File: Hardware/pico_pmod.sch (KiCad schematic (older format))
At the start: 6 parts, among them J1 Conn_02x15_Odd_Even, U1 Pico

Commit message: add power pin headers and initial layout work
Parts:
- J? (x3): footprint (none) -> Connector_PinHeader_2.54mm:PinHeader_1x02_P2.54mm_Vertical
- J?: value Conn_01x02 -> Conn_01x03; footprint (none) -> Connector_PinHeader_2.54mm:PinHeader_1x03_P2.54mm_Vertical; symbol Connector_Generic:Conn_01x02 -> Connector_Generic:Conn_01x03
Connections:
- net +3V3: now also J?.1 (Pin_1), J?.3 (Pin_3)
- net +5V: now also J?.1 (Pin_1), J?.1 (Pin_1)
- net GND: now also J?.1 (Pin_1)
- net Pic_VSYS renamed Pico_VSYS
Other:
- note added: "3V3_en connects to the SMPS enable pin\nto de-power the pico pull to ground\n(Pi Pico Datasheet, Page 8)"
- note added: "Direct input from the \nMicro USB connector approx 5v"
- note added: "Main System input voltage, \ncan be in the range of 1.8V to 5.5V"
- note added: "The main 3v3 supply from the pico, \nupto 300mA max draw"
- moved on the sheet: J?
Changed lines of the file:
@@
 Text GLabel 6650 4400 2    50   Input ~ 0
 Pico_3V3
-Text GLabel 8150 4400 2    50   Input ~ 0
+Text GLabel 9100 4500 2    50   Input ~ 0
 Pico_3v3_EN
 $Comp
 L Connector_Generic:Conn_01x02 J?
 U 1 1 607A9E26
-P 7950 4200
-F 0 "J?" V 7950 4400 50  0000 R CNN
-F 1 "Conn_01x02" V 7950 3950 50  0000 R CNN
-F 2 "" H 7950 4200 50  0001 C CNN
-F 3 "~" H 7950 4200 50  0001 C CNN
-	1    7950 4200
+P 8900 4300
+F 0 "J?" V 8900 4500 50  0000 R CNN
+F 1 "Conn_01x02" V 8900 4050 50  0000 R CNN
+F 2 "Connector_PinHeader_2.54mm:PinHeader_1x02_P2.54mm_Vertical" H 8900 4300 50  0001 C CNN
+F 3 "~" H 8900 4300 50  0001 C CNN
+	1    8900 4300
 	0    -1   -1   0
 $EndComp
@@
 F 0 "J?" V 6400 4400 50  0000 R CNN
 F 1 "Conn_01x02" V 6400 3950 50  0000 R CNN
-F 2 "" H 6400 4200 50  0001 C CNN
+F 2 "Connector_PinHeader_2.54mm:PinHeader_1x02_P2.54mm_Vertical" H 6400 4200 50  0001 C CNN
 F 3 "~" H 6400 4200 50  0001 C CNN
 	1    6400 4200
@@
 Pico_VBUS
 Text GLabel 4650 1800 2    50   Input ~ 0
-Pic_VSYS
+Pico_VSYS
 Wire Wire Line
 	4400 1700 4650 1700
@@
 	6500 4400 6650 4400
 Wire Wire Line
-	8050 4400 8150 4400
-Text GLabel 8200 5100 2    50   Input ~ 0
+	9000 4500 9100 4500
+Text GLabel 6600 5900 2    50   Input ~ 0
 Pico_VBUS
-Text GLabel 6650 5150 2    50   Input ~ 0
-Pic_VSYS
-$Comp
-L Connector_Generic:Conn_01x02 J?
+Text GLabel 9050 5750 3    50   Input ~ 0
+Pico_VSYS
+$Comp
+L Connector_Generic:Conn_01x03 J?
 U 1 1 607BB4AD
-P 6400 4950
-F 0 "J?" V 6400 5150 50  0000 R CNN
-F 1 "Conn_01x02" V 6400 4700 50  0000 R CNN
-F 2 "" H 6400 4950 50  0001 C CNN
-F 3 "~" H 6400 4950 50  0001 C CNN
-	1    6400 4950
+P 9050 5550
+F 0 "J?" V 9050 5750 50  0000 R CNN
+F 1 "Conn_01x03" V 9050 5300 50  0000 R CNN
+F 2 "Connector_PinHeader_2.54mm:PinHeader_1x03_P2.54mm_Vertical" H 9050 5550 50  0001 C CNN
+F 3 "~" H 9050 5550 50  0001 C CNN
+	1    9050 5550
 	0    -1   -1   0
 $EndComp
@@
 L Connector_Generic:Conn_01x02 J?
 U 1 1 607BCE20
-P 7950 4900
-F 0 "J?" V 7950 5100 50  0000 R CNN
-F 1 "Conn_01x02" V 7950 4650 50  0000 R CNN
-F 2 "" H 7950 4900 50  0001 C CNN
-F 3 "~" H 7950 4900 50  0001 C CNN
-	1    7950 4900
-	0    -1   -1   0
-$EndComp
-Wire Wire Line
-	6650 5150 6500 5150
-Wire Wire Line
-	8200 5100 8050 5100
+P 6350 5700
+F 0 "J?" V 6350 5900 50  0000 R CNN
+F 1 "Conn_01x02" V 6350 5450 50  0000 R CNN
+F 2 "Connector_PinHeader_2.54mm:PinHeader_1x02_P2.54mm_Vertical" H 6350 5700 50  0001 C CNN
+F 3 "~" H 6350 5700 50  0001 C CNN
+	1    6350 5700
+	0    -1   -1   0
+$EndComp
+Wire Wire Line
+	6600 5900 6450 5900
 Text GLabel 6800 3250 0    50   Input ~ 0
 GPIO_14
@@
 Wire Wire Line
 	7100 2150 6800 2150
+$Comp
+L power:+5V #PWR?
+U 1 1 60789CE8
+P 8700 5750
+F 0 "#PWR?" H 8700 5600 50  0001 C CNN
+F 1 "+5V" V 8715 5878 50  0000 L CNN
+F 2 "" H 8700 5750 50  0001 C CNN
+F 3 "" H 8700 5750 50  0001 C CNN
+	1    8700 5750
+	0    -1   -1   0
+$EndComp
+Text Notes 5800 6150 0    50   ~ 0
+Direct input from the \nMicro USB connector approx 5v
+Text Notes 8650 6400 0    50   ~ 0
+Main System input voltage, \ncan be in the range of 1.8V to 5.5V
+Text Notes 8600 4850 0    50   ~ 0
+3V3_en connects to the SMPS enable pin\nto de-power the pico pull to ground\n(Pi Pico Datasheet, Page 8)
+Text Notes 5900 4750 0    50   ~ 0
+The main 3v3 supply from the pico, \nupto 300mA max draw
+$Comp
+L power:+3.3V #PWR?
+U 1 1 607A1448
+P 9350 5750
+F 0 "#PWR?" H 9350 5600 50  0001 C CNN
+F 1 "+3.3V" V 9365 5878 50  0000 L CNN
+F 2 "" H 9350 5750 50  0001 C CNN
+F 3 "" H 9350 5750 50  0001 C CNN
+	1    9350 5750
+	0    1    1    0
+$EndComp
+Wire Wire Line
+	9150 5750 9350 5750
+Wire Wire Line
+	8950 5750 8700 5750
+$Comp
+L power:+5V #PWR?
+U 1 1 607A75D5
+P 6200 5900
+F 0 "#PWR?" H 6200 5750 50  0001 C CNN
+F 1 "+5V" V 6215 6028 50  0000 L CNN
+F 2 "" H 6200 5900 50  0001 C CNN
+F 3 "" H 6200 5900 50  0001 C CNN
+	1    6200 5900
+	0    -1   -1   0
+$EndComp
+Wire Wire Line
+	6350 5900 6200 5900
+$Comp
+L power:+3.3V #PWR?
+U 1 1 607ACAD5
+P 6300 4400
+F 0 "#PWR?" H 6300 4250 50  0001 C CNN
+F 1 "+3.3V" V 6315 4528 50  0000 L CNN
+F 2 "" H 6300 4400 50  0001 C CNN
+F 3 "" H 6300 4400 50  0001 C CNN
+	1    6300 4400
+	0    -1   -1   0
+$EndComp
+Wire Wire Line
+	6300 4400 6400 4400
+$Comp
+L power:GND #PWR?
+U 1 1 607B85C8
+P 8750 4500
+F 0 "#PWR?" H 8750 4250 50  0001 C CNN
+F 1 "GND" V 8755 4372 50  0000 R CNN
+F 2 "" H 8750 4500 50  0001 C CNN
+F 3 "" H 8750 4500 50  0001 C CNN
+	1    8750 4500
+	0    1    1    0
+$EndComp
+Wire Wire Line
+	8900 4500 8750 4500
 $EndSCHEMATC

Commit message: finish layout, start of silk screen
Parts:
- gave numbers to parts that had none: 4
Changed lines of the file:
@@
 $EndComp
 $Comp
-L power:GND #PWR?
+L power:GND #PWR0101
 U 1 1 60786DCD
 P 6800 1950
-F 0 "#PWR?" H 6800 1700 50  0001 C CNN
+F 0 "#PWR0101" H 6800 1700 50  0001 C CNN
 F 1 "GND" V 6805 1822 50  0000 R CNN
 F 2 "" H 6800 1950 50  0001 C CNN
@@
 $EndComp
 $Comp
-L power:+3.3V #PWR?
+L power:+3.3V #PWR0102
 U 1 1 6078774E
 P 6800 1850
-F 0 "#PWR?" H 6800 1700 50  0001 C CNN
+F 0 "#PWR0102" H 6800 1700 50  0001 C CNN
 F 1 "+3.3V" V 6815 1978 50  0000 L CNN
 F 2 "" H 6800 1850 50  0001 C CNN
@@
 $EndComp
 $Comp
-L power:GND #PWR?
+L power:GND #PWR0103
 U 1 1 60788D6C
 P 7950 1950
-F 0 "#PWR?" H 7950 1700 50  0001 C CNN
+F 0 "#PWR0103" H 7950 1700 50  0001 C CNN
 F 1 "GND" V 7955 1822 50  0000 R CNN
 F 2 "" H 7950 1950 50  0001 C CNN
@@
 $EndComp
 $Comp
-L power:+3.3V #PWR?
+L power:+3.3V #PWR0104
 U 1 1 60788D72
 P 7950 1850
-F 0 "#PWR?" H 7950 1700 50  0001 C CNN
+F 0 "#PWR0104" H 7950 1700 50  0001 C CNN
 F 1 "+3.3V" V 7965 1978 50  0000 L CNN
 F 2 "" H 7950 1850 50  0001 C CNN
@@
 $EndComp
 $Comp
-L power:GND #PWR?
+L power:GND #PWR0105
 U 1 1 60789DB6
 P 7950 2850
-F 0 "#PWR?" H 7950 2600 50  0001 C CNN
+F 0 "#PWR0105" H 7950 2600 50  0001 C CNN
 F 1 "GND" V 7955 2722 50  0000 R CNN
 F 2 "" H 7950 2850 50  0001 C CNN
@@
 $EndComp
 $Comp
-L power:+3.3V #PWR?
+L power:+3.3V #PWR0106
 U 1 1 60789DBC
 P 7950 2750
-F 0 "#PWR?" H 7950 2600 50  0001 C CNN
+F 0 "#PWR0106" H 7950 2600 50  0001 C CNN
 F 1 "+3.3V" V 7965 2878 50  0000 L CNN
 F 2 "" H 7950 2750 50  0001 C CNN
@@
 $EndComp
 $Comp
-L power:GND #PWR?
+L power:GND #PWR0107
 U 1 1 6078AF24
 P 6800 2850
-F 0 "#PWR?" H 6800 2600 50  0001 C CNN
+F 0 "#PWR0107" H 6800 2600 50  0001 C CNN
 F 1 "GND" V 6805 2722 50  0000 R CNN
 F 2 "" H 6800 2850 50  0001 C CNN
@@
 $EndComp
 $Comp
-L power:+3.3V #PWR?
+L power:+3.3V #PWR0108
 U 1 1 6078AF2A
 P 6800 2750
-F 0 "#PWR?" H 6800 2600 50  0001 C CNN
+F 0 "#PWR0108" H 6800 2600 50  0001 C CNN
 F 1 "+3.3V" V 6815 2878 50  0000 L CNN
 F 2 "" H 6800 2750 50  0001 C CNN
@@
 $EndComp
 $Comp
-L power:+5V #PWR?
+L power:+5V #PWR0109
 U 1 1 6078B324
 P 6800 2550
-F 0 "#PWR?" H 6800 2400 50  0001 C CNN
+F 0 "#PWR0109" H 6800 2400 50  0001 C CNN
 F 1 "+5V" V 6815 2678 50  0000 L CNN
 F 2 "" H 6800 2550 50  0001 C CNN
@@
 $EndComp
 $Comp
-L power:GND #PWR?
+L power:GND #PWR0110
 U 1 1 6078D676
 P 2800 1900
-F 0 "#PWR?" H 2800 1650 50  0001 C CNN
+F 0 "#PWR0110" H 2800 1650 50  0001 C CNN
 F 1 "GND" V 2805 1772 50  0000 R CNN
 F 2 "" H 2800 1900 50  0001 C CNN
@@
 $EndComp
 $Comp
-L power:GND #PWR?
+L power:GND #PWR0111
 U 1 1 6078E41F
 P 2800 2400
-F 0 "#PWR?" H 2800 2150 50  0001 C CNN
+F 0 "#PWR0111" H 2800 2150 50  0001 C CNN
 F 1 "GND" V 2805 2272 50  0000 R CNN
 F 2 "" H 2800 2400 50  0001 C CNN
@@
 $EndComp
 $Comp
-L power:GND #PWR?
+L power:GND #PWR0112
 U 1 1 6078E7A0
 P 2800 2900
-F 0 "#PWR?" H 2800 2650 50  0001 C CNN
+F 0 "#PWR0112" H 2800 2650 50  0001 C CNN
 F 1 "GND" V 2805 2772 50  0000 R CNN
 F 2 "" H 2800 2900 50  0001 C CNN
@@
 $EndComp
 $Comp
-L power:GND #PWR?
+L power:GND #PWR0113
 U 1 1 6078ED6D
 P 2800 3400
-F 0 "#PWR?" H 2800 3150 50  0001 C CNN
+F 0 "#PWR0113" H 2800 3150 50  0001 C CNN
 F 1 "GND" V 2805 3272 50  0000 R CNN
 F 2 "" H 2800 3400 50  0001 C CNN
@@
 $EndComp
 $Comp
-L power:GND #PWR?
+L power:GND #PWR0114
 U 1 1 6078F779
 P 4550 3400
-F 0 "#PWR?" H 4550 3150 50  0001 C CNN
+F 0 "#PWR0114" H 4550 3150 50  0001 C CNN
 F 1 "GND" V 4555 3272 50  0000 R CNN
 F 2 "" H 4550 3400 50  0001 C CNN
@@
 $EndComp
 $Comp
-L power:GND #PWR?
+L power:GND #PWR0115
 U 1 1 6078FEE8
 P 4550 2900
-F 0 "#PWR?" H 4550 2650 50  0001 C CNN
+F 0 "#PWR0115" H 4550 2650 50  0001 C CNN
 F 1 "GND" V 4555 2772 50  0000 R CNN
 F 2 "" H 4550 2900 50  0001 C CNN
@@
 $EndComp
 $Comp
-L power:GND #PWR?
+L power:GND #PWR0116
 U 1 1 60790DB5
 P 4600 1900
-F 0 "#PWR?" H 4600 1650 50  0001 C CNN
+F 0 "#PWR0116" H 4600 1650 50  0001 C CNN
 F 1 "GND" V 4605 1772 50  0000 R CNN
 F 2 "" H 4600 1900 50  0001 C CNN
@@
 	7600 1950 7950 1950
 $Comp
-L power:GND #PWR?
+L power:GND #PWR0117
 U 1 1 60794128
 P 3700 3900
-F 0 "#PWR?" H 3700 3650 50  0001 C CNN
+F 0 "#PWR0117" H 3700 3650 50  0001 C CNN
 F 1 "GND" V 3705 3772 50  0000 R CNN
 F 2 "" H 3700 3900 50  0001 C CNN
@@
 	4400 1900 4600 1900
 $Comp
-L power:GND #PWR?
+L power:GND #PWR0118
 U 1 1 60796681
 P 7950 2550
-F 0 "#PWR?" H 7950 2300 50  0001 C CNN
+F 0 "#PWR0118" H 7950 2300 50  0001 C CNN
 F 1 "GND" V 7955 2422 50  0000 R CNN
 F 2 "" H 7950 2550 50  0001 C CNN
@@
 Pico_3v3_EN
 $Comp
-L Connector_Generic:Conn_01x02 J?
+L Connector_Generic:Conn_01x02 J4
 U 1 1 607A9E26
 P 8900 4300
-F 0 "J?" V 8900 4500 50  0000 R CNN
+F 0 "J4" V 8900 4500 50  0000 R CNN
 F 1 "Conn_01x02" V 8900 4050 50  0000 R CNN
 F 2 "Connector_PinHeader_2.54mm:PinHeader_1x02_P2.54mm_Vertical" H 8900 4300 50  0001 C CNN
@@
 $EndComp
 $Comp
-L Connector_Generic:Conn_01x02 J?
+L Connector_Generic:Conn_01x02 J3
 U 1 1 607B1D77
 P 6400 4200
-F 0 "J?" V 6400 4400 50  0000 R CNN
+F 0 "J3" V 6400 4400 50  0000 R CNN
 F 1 "Conn_01x02" V 6400 3950 50  0000 R CNN
 F 2 "Connector_PinHeader_2.54mm:PinHeader_1x02_P2.54mm_Vertical" H 6400 4200 50  0001 C CNN
@@
 Pico_VSYS
 $Comp
-L Connector_Generic:Conn_01x03 J?
+L Connector_Generic:Conn_01x03 J5
 U 1 1 607BB4AD
 P 9050 5550
-F 0 "J?" V 9050 5750 50  0000 R CNN
+F 0 "J5" V 9050 5750 50  0000 R CNN
 F 1 "Conn_01x03" V 9050 5300 50  0000 R CNN
 F 2 "Connector_PinHeader_2.54mm:PinHeader_1x03_P2.54mm_Vertical" H 9050 5550 50  0001 C CNN
@@
 $EndComp
 $Comp
-L Connector_Generic:Conn_01x02 J?
+L Connector_Generic:Conn_01x02 J2
 U 1 1 607BCE20
 P 6350 5700
-F 0 "J?" V 6350 5900 50  0000 R CNN
+F 0 "J2" V 6350 5900 50  0000 R CNN
 F 1 "Conn_01x02" V 6350 5450 50  0000 R CNN
 F 2 "Connector_PinHeader_2.54mm:PinHeader_1x02_P2.54mm_Vertical" H 6350 5700 50  0001 C CNN
@@
 	7100 2150 6800 2150
 $Comp
-L power:+5V #PWR?
+L power:+5V #PWR0119
 U 1 1 60789CE8
 P 8700 5750
-F 0 "#PWR?" H 8700 5600 50  0001 C CNN
+F 0 "#PWR0119" H 8700 5600 50  0001 C CNN
 F 1 "+5V" V 8715 5878 50  0000 L CNN
 F 2 "" H 8700 5750 50  0001 C CNN
@@
 The main 3v3 supply from the pico, \nupto 300mA max draw
 $Comp
-L power:+3.3V #PWR?
+L power:+3.3V #PWR0120
 U 1 1 607A1448
 P 9350 5750
-F 0 "#PWR?" H 9350 5600 50  0001 C CNN
+F 0 "#PWR0120" H 9350 5600 50  0001 C CNN
 F 1 "+3.3V" V 9365 5878 50  0000 L CNN
 F 2 "" H 9350 5750 50  0001 C CNN
@@
 	8950 5750 8700 5750
 $Comp
-L power:+5V #PWR?
+L power:+5V #PWR0121
 U 1 1 607A75D5
 P 6200 5900
-F 0 "#PWR?" H 6200 5750 50  0001 C CNN
+F 0 "#PWR0121" H 6200 5750 50  0001 C CNN
 F 1 "+5V" V 6215 6028 50  0000 L CNN
 F 2 "" H 6200 5900 50  0001 C CNN
@@
 	6350 5900 6200 5900
 $Comp
-L power:+3.3V #PWR?
+L power:+3.3V #PWR0122
 U 1 1 607ACAD5
 P 6300 4400
-F 0 "#PWR?" H 6300 4250 50  0001 C CNN
+F 0 "#PWR0122" H 6300 4250 50  0001 C CNN
 F 1 "+3.3V" V 6315 4528 50  0000 L CNN
 F 2 "" H 6300 4400 50  0001 C CNN
@@
 	6300 4400 6400 4400
 $Comp
-L power:GND #PWR?
+L power:GND #PWR0123
 U 1 1 607B85C8
 P 8750 4500
-F 0 "#PWR?" H 8750 4250 50  0001 C CNN
+F 0 "#PWR0123" H 8750 4250 50  0001 C CNN
 F 1 "GND" V 8755 4372 50  0000 R CNN
 F 2 "" H 8750 4500 50  0001 C CNN

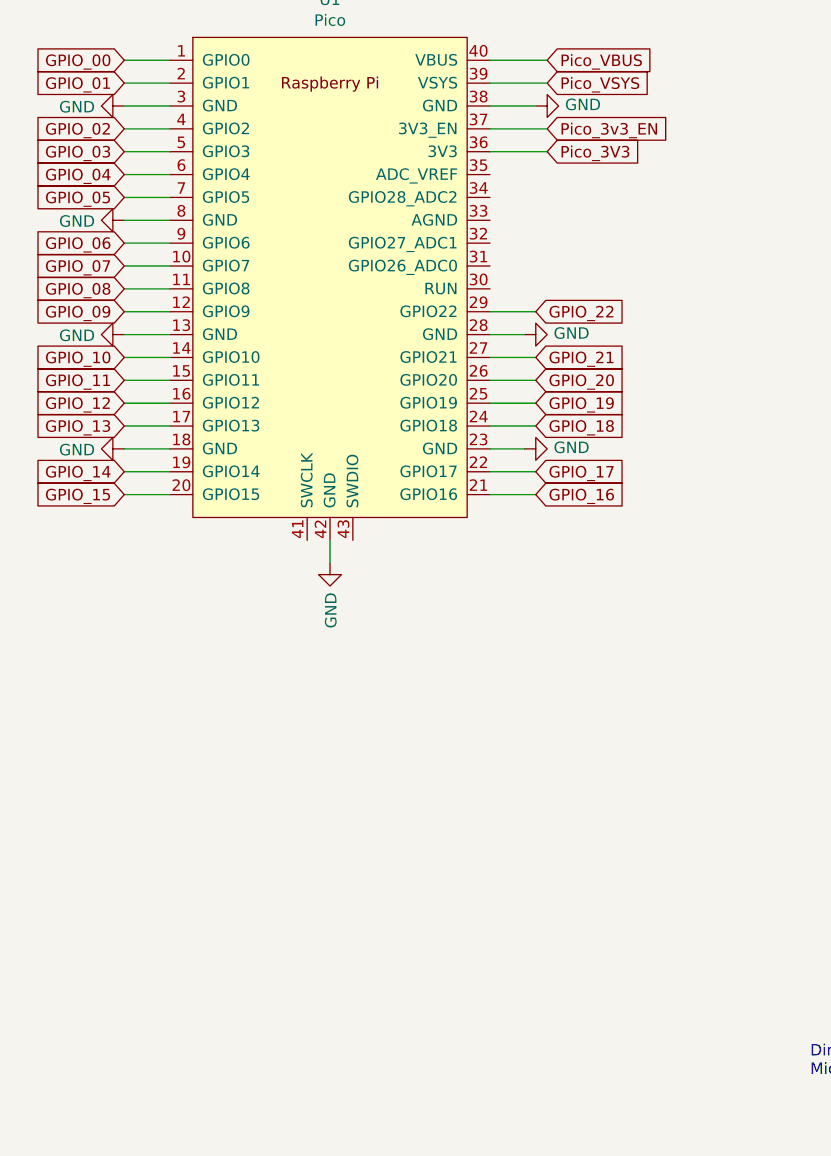
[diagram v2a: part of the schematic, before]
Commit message: breakout ADC inputs to pins
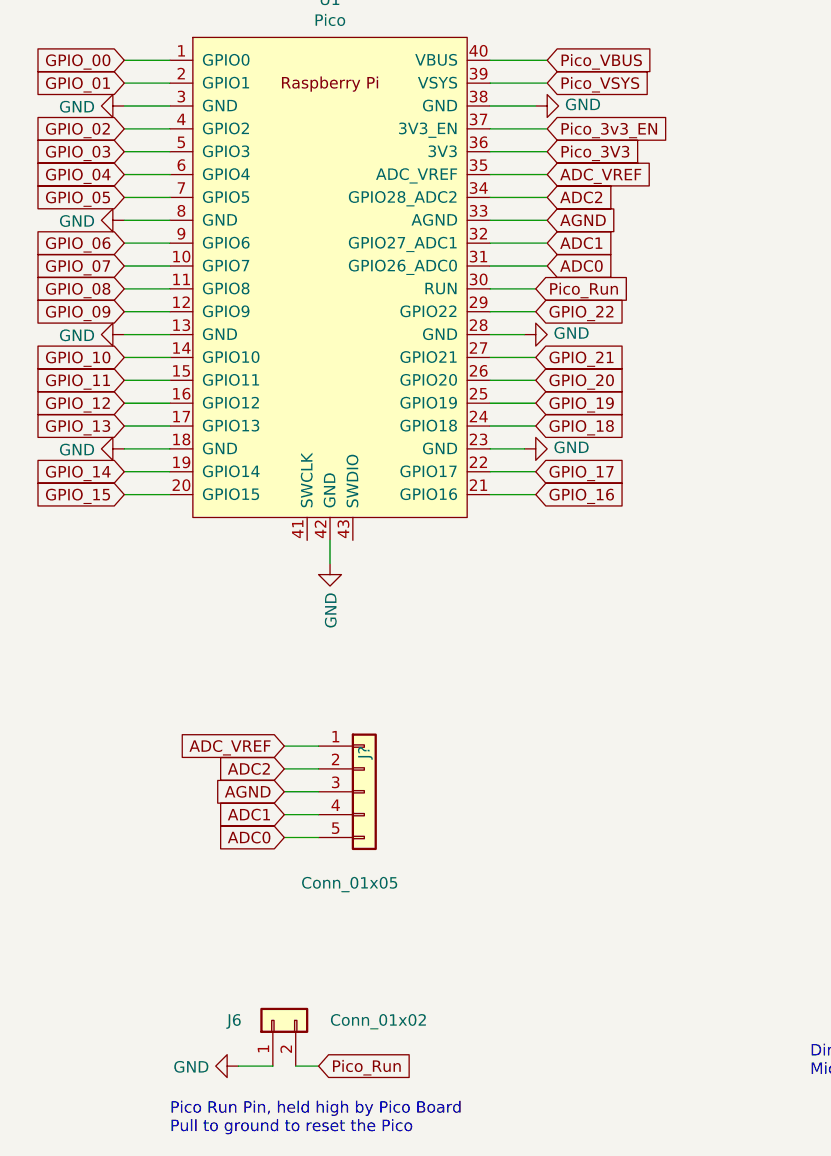
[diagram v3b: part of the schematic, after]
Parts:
- added J6: Conn_01x02, Connector_PinHeader_2.54mm:PinHeader_1x02_P2.54mm_Vertical, symbol Connector_Generic:Conn_01x02
- added J?: Conn_01x05, Connector_PinHeader_2.54mm:PinHeader_1x05_P2.54mm_Vertical, symbol Connector_Generic:Conn_01x05
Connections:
- net GND: now also J6.1 (Pin_1)
- net Pico_Run: now reaches U1.30 (RUN)
- net Pico_Run: now also J6.2 (Pin_2)
- net ADC0: now reaches U1.31 (GPIO26_ADC0)
- net ADC0: now also J?.5 (Pin_5)
- net ADC1: now reaches U1.32 (GPIO27_ADC1)
- net ADC1: now also J?.4 (Pin_4)
- net AGND: now reaches U1.33 (AGND)
- net AGND: now also J?.3 (Pin_3)
- net ADC2: now reaches U1.34 (GPIO28_ADC2)
- net ADC2: now also J?.2 (Pin_2)
- net ADC_VREF: now reaches U1.35 (ADC_VREF)
- net ADC_VREF: now also J?.1 (Pin_1)
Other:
- note added: "Pico Run Pin, held high by Pico Board\nPull to ground to reset the Pico"
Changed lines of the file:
@@
 Wire Wire Line
 	8900 4500 8750 4500
+Text GLabel 3650 6100 2    50   Input ~ 0
+Pico_Run
+$Comp
+L Connector_Generic:Conn_01x02 J6
+U 1 1 607985C4
+P 3450 5900
+F 0 "J6" V 3450 6100 50  0000 R CNN
+F 1 "Conn_01x02" V 3450 5650 50  0000 R CNN
+F 2 "Connector_PinHeader_2.54mm:PinHeader_1x02_P2.54mm_Vertical" H 3450 5900 50  0001 C CNN
+F 3 "~" H 3450 5900 50  0001 C CNN
+	1    3450 5900
+	0    -1   -1   0
+$EndComp
+Wire Wire Line
+	3550 6100 3650 6100
+Text Notes 3000 6400 0    50   ~ 0
+Pico Run Pin, held high by Pico Board\nPull to ground to reset the Pico
+$Comp
+L power:GND #PWR0124
+U 1 1 607985CC
+P 3300 6100
+F 0 "#PWR0124" H 3300 5850 50  0001 C CNN
+F 1 "GND" V 3305 5972 50  0000 R CNN
+F 2 "" H 3300 6100 50  0001 C CNN
+F 3 "" H 3300 6100 50  0001 C CNN
+	1    3300 6100
+	0    1    1    0
+$EndComp
+Wire Wire Line
+	3450 6100 3300 6100
+Text GLabel 4600 2700 2    50   Input ~ 0
+Pico_Run
+Wire Wire Line
+	4600 2700 4400 2700
+$Comp
+L Connector_Generic:Conn_01x05 J?
+U 1 1 607A6E5A
+P 3850 4900
+F 0 "J?" V 3850 5100 50  0000 R CNN
+F 1 "Conn_01x05" H 4000 4500 50  0000 R CNN
+F 2 "Connector_PinHeader_2.54mm:PinHeader_1x05_P2.54mm_Vertical" H 3850 4900 50  0001 C CNN
+F 3 "~" H 3850 4900 50  0001 C CNN
+	1    3850 4900
+	1    0    0    -1
+$EndComp
+Text GLabel 3500 4700 0    50   Input ~ 0
+ADC_VREF
+Text GLabel 3500 4800 0    50   Input ~ 0
+ADC2
+Text GLabel 3500 4900 0    50   Input ~ 0
+AGND
+Text GLabel 3500 5000 0    50   Input ~ 0
+ADC1
+Text GLabel 3500 5100 0    50   Input ~ 0
+ADC0
+Wire Wire Line
+	3500 4700 3650 4700
+Wire Wire Line
+	3500 4800 3650 4800
+Wire Wire Line
+	3500 4900 3650 4900
+Wire Wire Line
+	3650 5000 3500 5000
+Wire Wire Line
+	3500 5100 3650 5100
+Text GLabel 4650 2200 2    50   Input ~ 0
+ADC_VREF
+Text GLabel 4650 2300 2    50   Input ~ 0
+ADC2
+Text GLabel 4650 2400 2    50   Input ~ 0
+AGND
+Text GLabel 4650 2500 2    50   Input ~ 0
+ADC1
+Text GLabel 4650 2600 2    50   Input ~ 0
+ADC0
+Wire Wire Line
+	4650 2200 4400 2200
+Wire Wire Line
+	4400 2300 4650 2300
+Wire Wire Line
+	4650 2400 4400 2400
+Wire Wire Line
+	4400 2500 4650 2500
+Wire Wire Line
+	4650 2600 4400 2600
 $EndSCHEMATC

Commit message: Minor circuit changes
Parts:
- gave numbers to parts that had none: 1
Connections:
- no-connect marks 0 -> 2
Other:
- note added: "ADC Connections Breakout\n"
- note added: "Duel Extended PMod Connector"
- note added: "Raspberry Pi Pico"
- moved on the sheet: J1, J2, J3, J4, J5, J6, J7, U1
